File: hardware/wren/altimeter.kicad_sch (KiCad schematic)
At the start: 40 parts, among them J1 USB_C_Receptacle_USB2.0_16P, J2 Conn_01x05_MountingPin, SW2 SW_SPDT, U1 nRF52833_QDxx, U2 MCP73832T-2, U3 BMP390L, U4 W25X40CLUXIG, U5 LIS2DH, Y1 32MHz

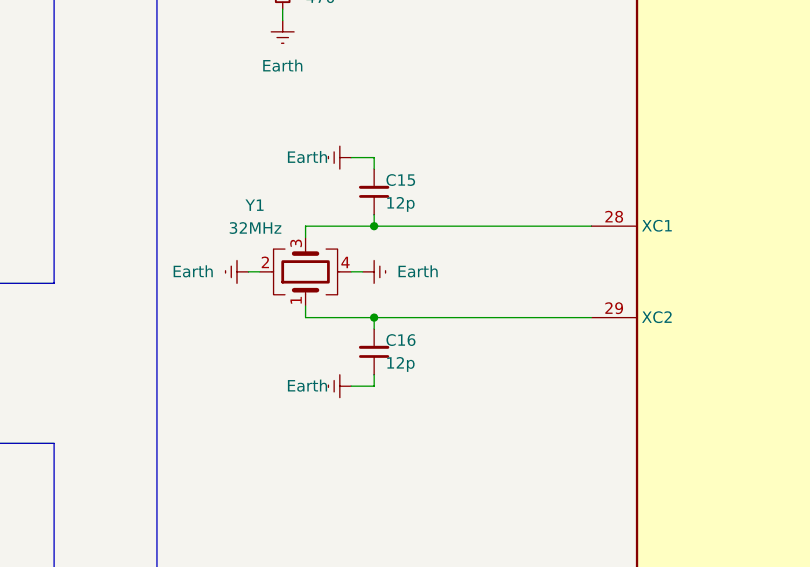
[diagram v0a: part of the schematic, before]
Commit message: Add bluetooth board
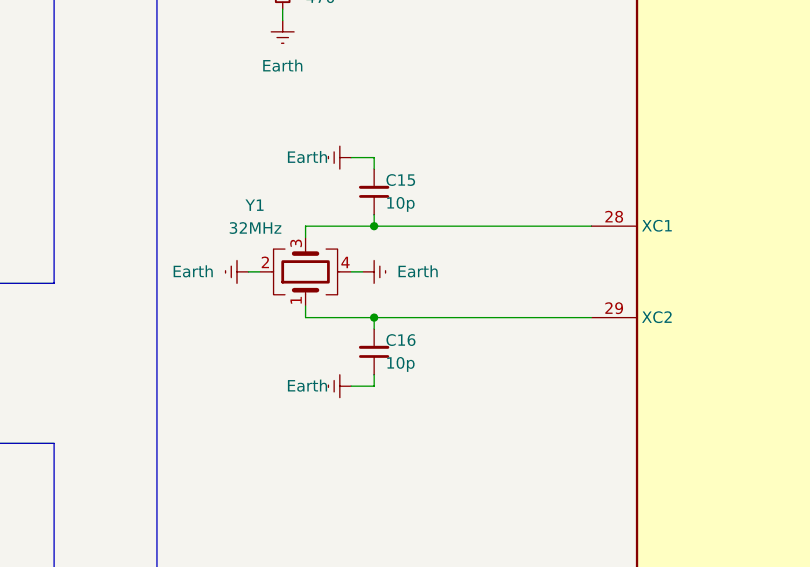
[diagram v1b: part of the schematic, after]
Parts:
- C15, C16: value 12p -> 10p; LCSC (none) -> C32949
- U3: LCSC C779278 -> C2684802
- Y1: LCSC C187794 -> C388796
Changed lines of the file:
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@@
 			)
 		)
-		(property "LCSC" "C187794"
+		(property "LCSC" "C388796"
 			(at 250.19 114.3 0)
 			(effects
@@
 			)
 		)
-		(property "LCSC" "C779278"
+		(property "LCSC" "C2684802"
 			(at 181.61 95.25 0)
 			(effects
@@
 			)
 		)
-		(property "Value" "12p"
+		(property "Value" "10p"
 			(at 259.08 124.46 0)
 			(effects
@@
 			)
 		)
-		(property "LCSC" ""
+		(property "LCSC" "C32949"
 			(at 257.81 123.19 0)
 			(effects
@@
 			)
 		)
-		(property "Value" "12p"
+		(property "Value" "10p"
 			(at 259.08 106.68 0)
 			(effects
@@
 			)
 		)
-		(property "LCSC" ""
+		(property "LCSC" "C32949"
 			(at 257.81 105.41 0)
 			(effects
